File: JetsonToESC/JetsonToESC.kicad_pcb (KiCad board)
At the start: 2 copper layers, 1 part, among them U1 ESP32-C3_SUPERMINI_TH

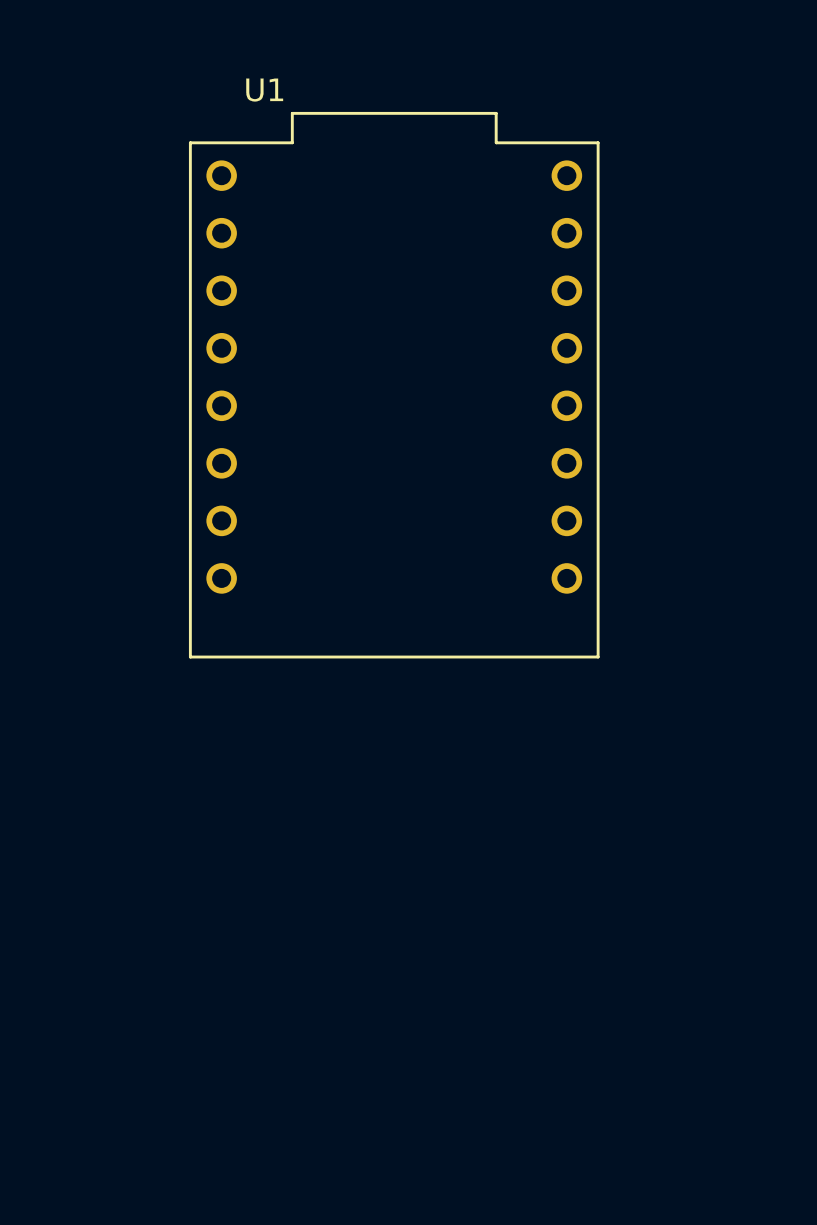
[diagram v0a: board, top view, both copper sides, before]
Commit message: Added footprints, connectors and cutout
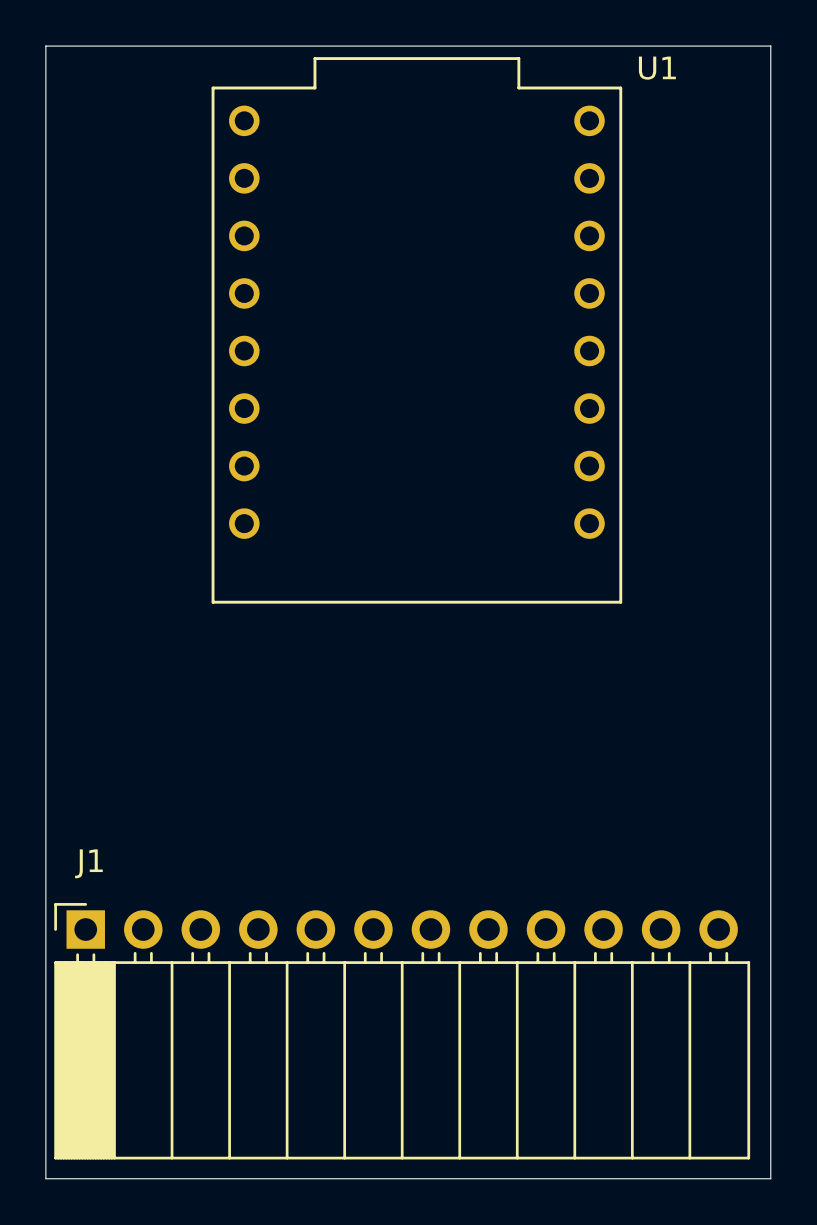
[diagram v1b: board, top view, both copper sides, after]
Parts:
- added J1: Conn_01x12, Connector_PinSocket_2.54mm:PinSocket_1x12_P2.54mm_Horizontal, F.Cu at (139.8, 119.0)
- moved U1 2.62 mm to (154.4, 93.2)
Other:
- board outline added: 32 x 50 mm

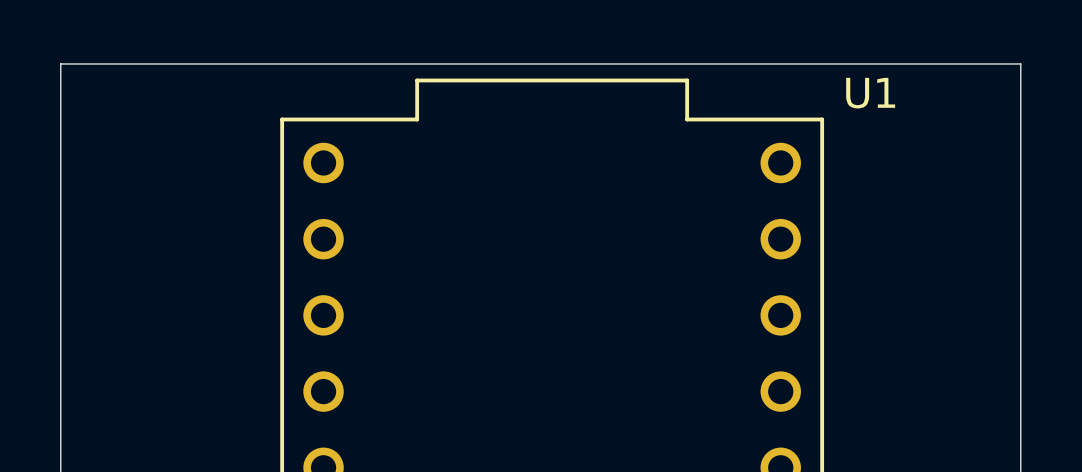
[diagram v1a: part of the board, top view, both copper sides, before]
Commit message: Added mechanic drills
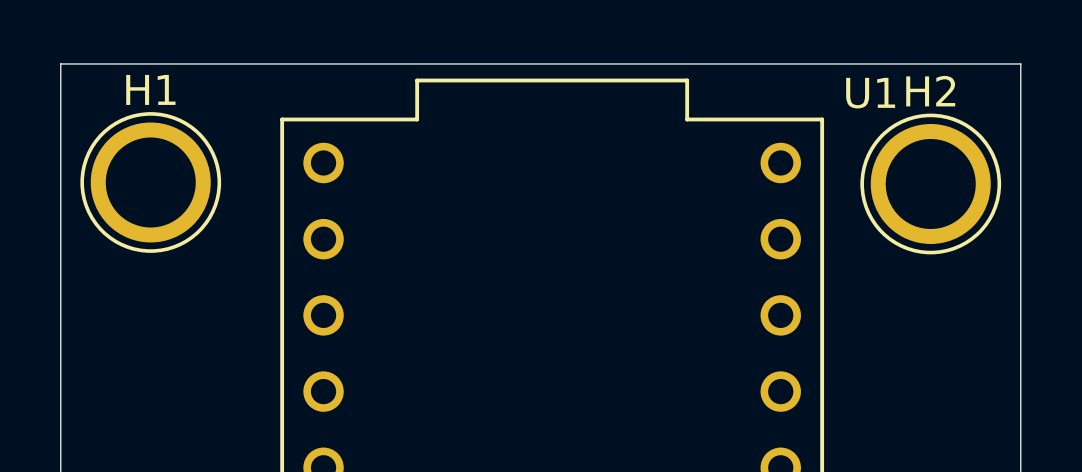
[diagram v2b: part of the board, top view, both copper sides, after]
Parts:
- added H1: MountingHole, TestPoint:TestPoint_Plated_Hole_D3.0mm, F.Cu at (141.0, 84.0)
- added H2: MountingHole, TestPoint:TestPoint_Plated_Hole_D3.0mm, F.Cu at (167.0, 84.0)
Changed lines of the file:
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@@
 	(net 27 "unconnected-(J1-Pin_7-Pad7)")
 	(net 28 "unconnected-(J1-Pin_6-Pad6)")
+	(footprint "TestPoint:TestPoint_Plated_Hole_D3.0mm"
+		(layer "F.Cu")
+		(at 141 83.95)
+		(descr "Plated Hole as test Point, diameter 3.0mm")
+		(tags "test point plated hole")
+		(property "Reference" "H1"
+			(at 0 -3.048 0)
+			(layer "F.SilkS")
+			(effects
+				(font
+					(size 1 1)
+					(thickness 0.15)
+				)
+			)
+		)
+		(property "Value" "MountingHole"
+			(at 0 3 0)
+			(layer "F.Fab")
+			(effects
+				(font
+					(size 1 1)
+					(thickness 0.15)
+				)
+			)
+		)
+		(property "Footprint" "TestPoint:TestPoint_Plated_Hole_D3.0mm"
+			(at 0 0 0)
+			(unlocked yes)
+			(layer "F.Fab")
+			(hide yes)
+			(effects
+				(font
+					(size 1.27 1.27)
+					(thickness 0.15)
+				)
+			)
+		)
+		(property "Datasheet" ""
+			(at 0 0 0)
+			(unlocked yes)
+			(layer "F.Fab")
+			(hide yes)
+			(effects
+				(font
+					(size 1.27 1.27)
+					(thickness 0.15)
+				)
+			)
+		)
+		(property "Description" "Mounting Hole without connection"
+			(at 0 0 0)
+			(unlocked yes)
+			(layer "F.Fab")
+			(hide yes)
+			(effects
+				(font
+					(size 1.27 1.27)
+					(thickness 0.15)
+				)
+			)
+		)
+		(property ki_fp_filters "MountingHole*")
+		(sheetname "Raíz")
+		(sheetfile "JetsonToESC.kicad_sch")
+		(attr exclude_from_pos_files exclude_from_bom)
+		(fp_circle
+			(center 0 0)
+			(end 0 -2.286)
+			(stroke
+				(width 0.12)
+				(type solid)
+			)
+			(fill none)
+			(layer "F.SilkS")
+		)
+		(fp_circle
+			(center 0 0)
+			(end 2.5 0)
+			(stroke
+				(width 0.05)
+				(type solid)
+			)
+			(fill none)
+			(layer "F.CrtYd")
+		)
+		(fp_text user "${REFERENCE}"
+			(at 0 -3.05 0)
+			(layer "F.Fab")
+			(effects
+				(font
+					(size 1 1)
+					(thickness 0.15)
+				)
+			)
+		)
+		(pad "1" thru_hole circle
+			(at 0 0)
+			(size 4 4)
+			(drill 3)
+			(layers "*.Cu" "*.Mask")
+			(remove_unused_layers no)
+		)
+	)
 	(footprint "Connector_PinSocket_2.54mm:PinSocket_1x12_P2.54mm_Horizontal"
 		(layer "F.Cu")
@@
 		)
 	)
+	(footprint "TestPoint:TestPoint_Plated_Hole_D3.0mm"
+		(layer "F.Cu")
+		(at 167 84)
+		(descr "Plated Hole as test Point, diameter 3.0mm")
+		(tags "test point plated hole")
+		(property "Reference" "H2"
+			(at 0 -3.048 0)
+			(layer "F.SilkS")
+			(effects
+				(font
+					(size 1 1)
+					(thickness 0.15)
+				)
+			)
+		)
+		(property "Value" "MountingHole"
+			(at 0 3 0)
+			(layer "F.Fab")
+			(effects
+				(font
+					(size 1 1)
+					(thickness 0.15)
+				)
+			)
+		)
+		(property "Footprint" "TestPoint:TestPoint_Plated_Hole_D3.0mm"
+			(at 0 0 0)
+			(unlocked yes)
+			(layer "F.Fab")
+			(hide yes)
+			(effects
+				(font
+					(size 1.27 1.27)
+					(thickness 0.15)
+				)
+			)
+		)
+		(property "Datasheet" ""
+			(at 0 0 0)
+			(unlocked yes)
+			(layer "F.Fab")
+			(hide yes)
+			(effects
+				(font
+					(size 1.27 1.27)
+					(thickness 0.15)
+				)
+			)
+		)
+		(property "Description" "Mounting Hole without connection"
+			(at 0 0 0)
+			(unlocked yes)
+			(layer "F.Fab")
+			(hide yes)
+			(effects
+				(font
+					(size 1.27 1.27)
+					(thickness 0.15)
+				)
+			)
+		)
+		(property ki_fp_filters "MountingHole*")
+		(sheetname "Raíz")
+		(sheetfile "JetsonToESC.kicad_sch")
+		(attr exclude_from_pos_files exclude_from_bom)
+		(fp_circle
+			(center 0 0)
+			(end 0 -2.286)
+			(stroke
+				(width 0.12)
+				(type solid)
+			)
+			(fill none)
+			(layer "F.SilkS")
+		)
+		(fp_circle
+			(center 0 0)
+			(end 2.5 0)
+			(stroke
+				(width 0.05)
+				(type solid)
+			)
+			(fill none)
+			(layer "F.CrtYd")
+		)
+		(fp_text user "${REFERENCE}"
+			(at 0 -3.05 0)
+			(layer "F.Fab")
+			(effects
+				(font
+					(size 1 1)
+					(thickness 0.15)
+				)
+			)
+		)
+		(pad "1" thru_hole circle
+			(at 0 0)
+			(size 4 4)
+			(drill 3)
+			(layers "*.Cu" "*.Mask")
+			(remove_unused_layers no)
+		)
+	)

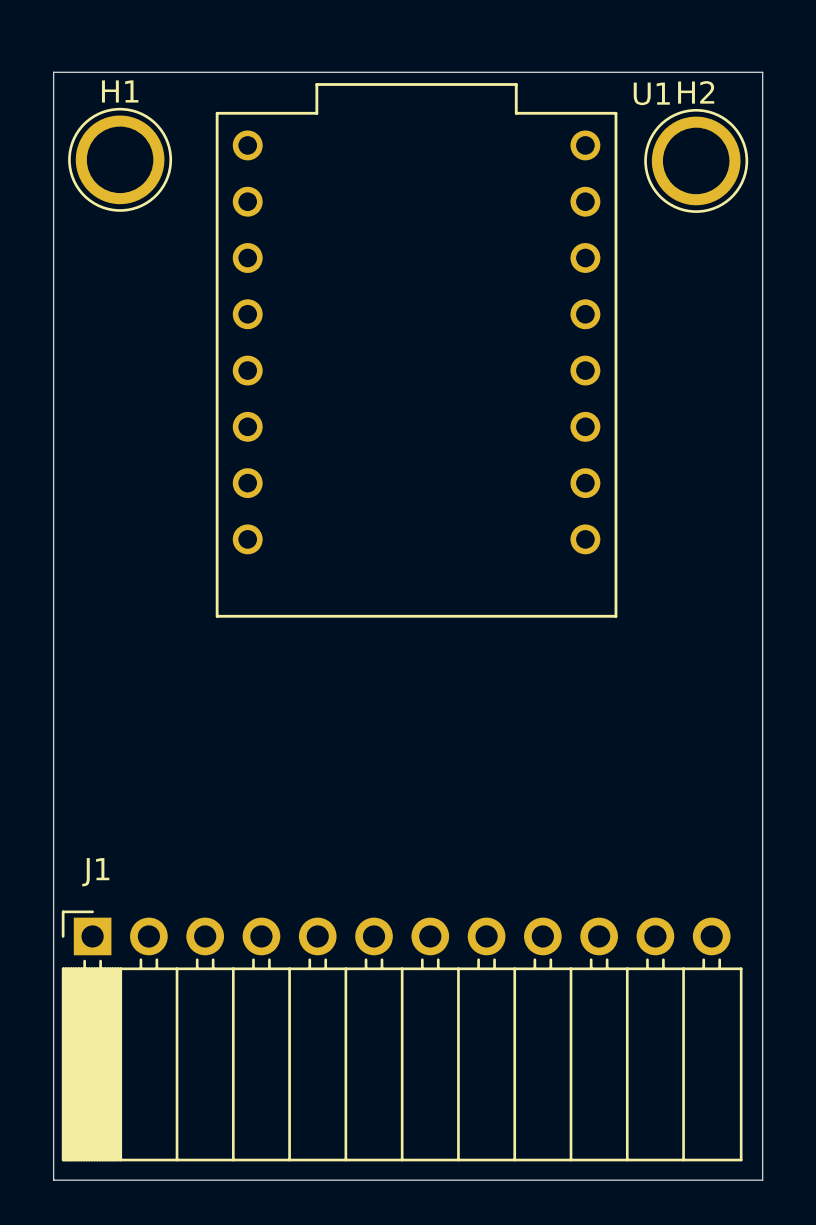
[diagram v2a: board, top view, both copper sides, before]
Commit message: Added most of components and preliminar routing
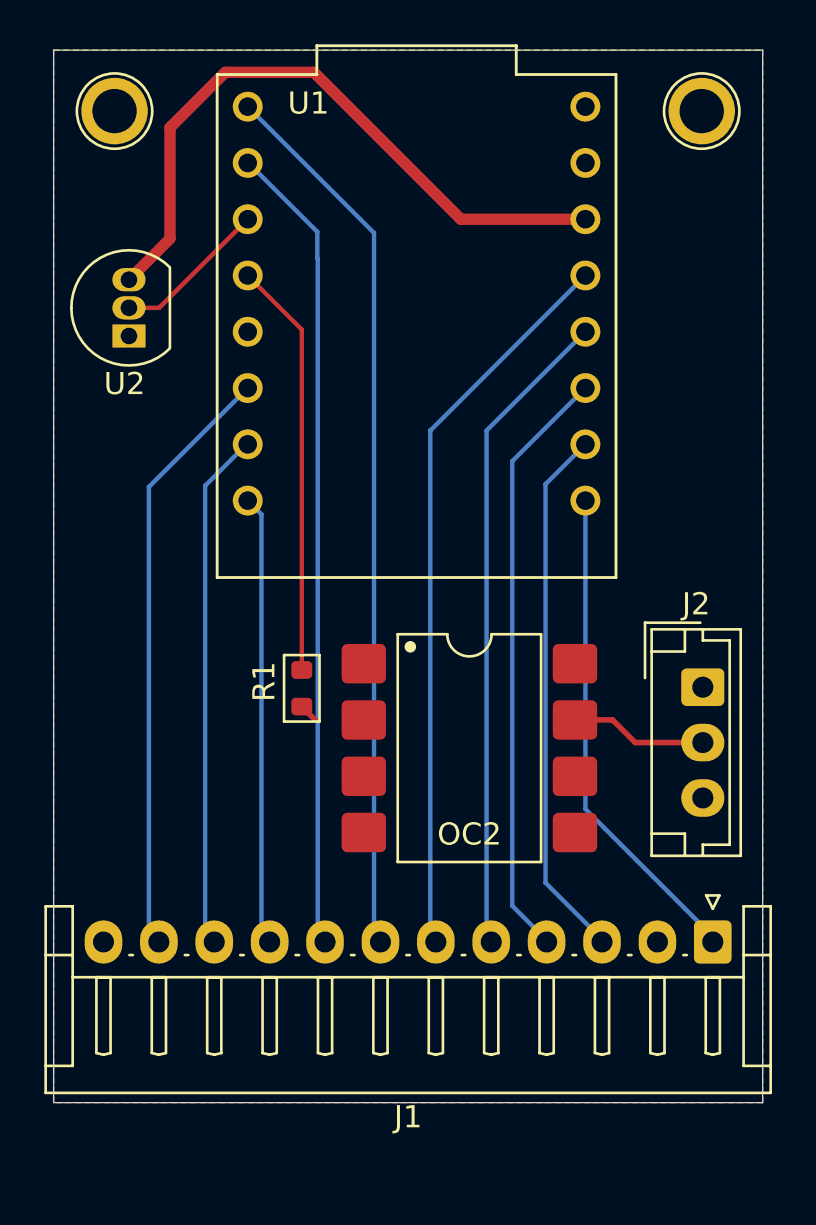
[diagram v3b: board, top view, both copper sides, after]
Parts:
- added J2: Conn_01x03, Connector_JST:JST_EH_B3B-EH-A_1x03_P2.50mm_Vertical, F.Cu at (167.3, 107.8)
- added OC2: 6N137-X007T, PCM_Package_DIP_AKL:SMDIP-8_W9.53mm, F.Cu at (156.8, 110.5)
- added R1: R, PCM_Resistor_SMD_AKL:R_0603_1608Metric, F.Cu at (149.2, 107.8)
- added U2: DS18B20, Package_TO_SOT_THT:TO-92_Inline, F.Cu at (141.4, 91.9)
- H1, H2: footprint TestPoint:TestPoint_Plated_Hole_D3.0mm -> TestPoint:TestPoint_Plated_Hole_D2.0mm
- J1: footprint Connector_PinSocket_2.54mm:PinSocket_1x12_P2.54mm_Horizontal -> Connector_JST:JST_EH_S12B-EH_1x12_P2.50mm_Horizontal
- moved J1 28.0 mm to (167.8, 119.2), turned to 180 degrees
- moved H2 2.26 mm to (167.2, 81.8)
- moved H1 2.21 mm to (140.8, 81.8)
- moved U1 1.75 mm to (154.4, 91.5)
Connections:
- J1 pad 1: unconnected-(J1-Pin_1-Pad1) -> LED_TEMP
- J1 pad 10: unconnected-(J1-Pin_10-Pad10) -> LED_BATT_MED
- J1 pad 11: unconnected-(J1-Pin_11-Pad11) -> LED_BATT_LOW
- J1 pad 12: unconnected-(J1-Pin_12-Pad12) -> 5V
- J1 pad 2: unconnected-(J1-Pin_2-Pad2) -> GND
- J1 pad 3: unconnected-(J1-Pin_3-Pad3) -> BUTTON_STOP
- J1 pad 4: unconnected-(J1-Pin_4-Pad4) -> BUTTON_25%
- J1 pad 5: unconnected-(J1-Pin_5-Pad5) -> BUTTON_50%
- J1 pad 6: unconnected-(J1-Pin_6-Pad6) -> BUTTON_75%
- J1 pad 7: unconnected-(J1-Pin_7-Pad7) -> BUTTON_100%
- J1 pad 8: unconnected-(J1-Pin_8-Pad8) -> LED_OVERCURRENT
- J1 pad 9: unconnected-(J1-Pin_9-Pad9) -> LED_BATT_HI
- U1 pad 0: unconnected-(U1-GPIO0-Pad0) -> LED_TEMP
- U1 pad 1: unconnected-(U1-GPIO1-Pad1) -> BUTTON_STOP
- U1 pad 10: unconnected-(U1-GPIO10-Pad10) -> LED_BATT_LOW
- U1 pad 2: unconnected-(U1-GPIO2-Pad2) -> BUTTON_25%
- U1 pad 20: unconnected-(U1-GPIO20-Pad20) -> LED_BATT_MED
- U1 pad 21: unconnected-(U1-GPIO21-Pad21) -> LED_BATT_HI
- U1 pad 3: unconnected-(U1-GPIO3-Pad3) -> BUTTON_50%
- U1 pad 3.3: unconnected-(U1-3V3-Pad3.3) -> 3V3
- U1 pad 4: unconnected-(U1-GPIO4-Pad4) -> BUTTON_75%
- U1 pad 5: unconnected-(U1-GPIO5-Pad5) -> BUTTON_100%
- U1 pad 5V: unconnected-(U1-Pad5V) -> VCC
- U1 pad 6: unconnected-(U1-GPIO6-Pad6) -> LED_OVERCURRENT
- U1 pad 7: unconnected-(U1-GPIO7-Pad7) -> TEMP_SENSE
- U1 pad 8: unconnected-(U1-GPIO8-Pad8) -> PWM
- U1 pad G: unconnected-(U1-GND-PadG) -> GND
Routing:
- net BUTTON_100%: track 0.00 -> 39.8 mm
- net LED_OVERCURRENT: track 0.00 -> 36.2 mm
- net BUTTON_75%: track 0.00 -> 32.7 mm
- net 3V3: track 0.00 -> 30.2 mm
- net BUTTON_50%: track 0.00 -> 29.1 mm
- net BUTTON_25%: track 0.00 -> 26.7 mm
- net LED_BATT_LOW: track 0.00 -> 26.6 mm
- net BUTTON_STOP: track 0.00 -> 24.0 mm
- net LED_BATT_MED: track 0.00 -> 23.0 mm
- net LED_TEMP: track 0.00 -> 22.0 mm
- net LED_BATT_HI: track 0.00 -> 19.9 mm
- net PWM: track 0.00 -> 18.8 mm
- net TEMP_SENSE: track 0.00 -> 7.02 mm
- net ESC_PWM: track 0.00 -> 6.19 mm
- net Net-(OC2-Pad2): track 0.00 -> 0.86 mm
- added copper zone on B.Cu, net GND
- added copper zone on F.Cu, net GND
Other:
- board size 32 x 50 mm -> 32 x 47.5 mm
